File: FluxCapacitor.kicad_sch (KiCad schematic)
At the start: 21 parts, among them J1 Jack-DC, U1 OKI-78SR-5_1.5-W36-C, U2 ESP32_DEVBOARD

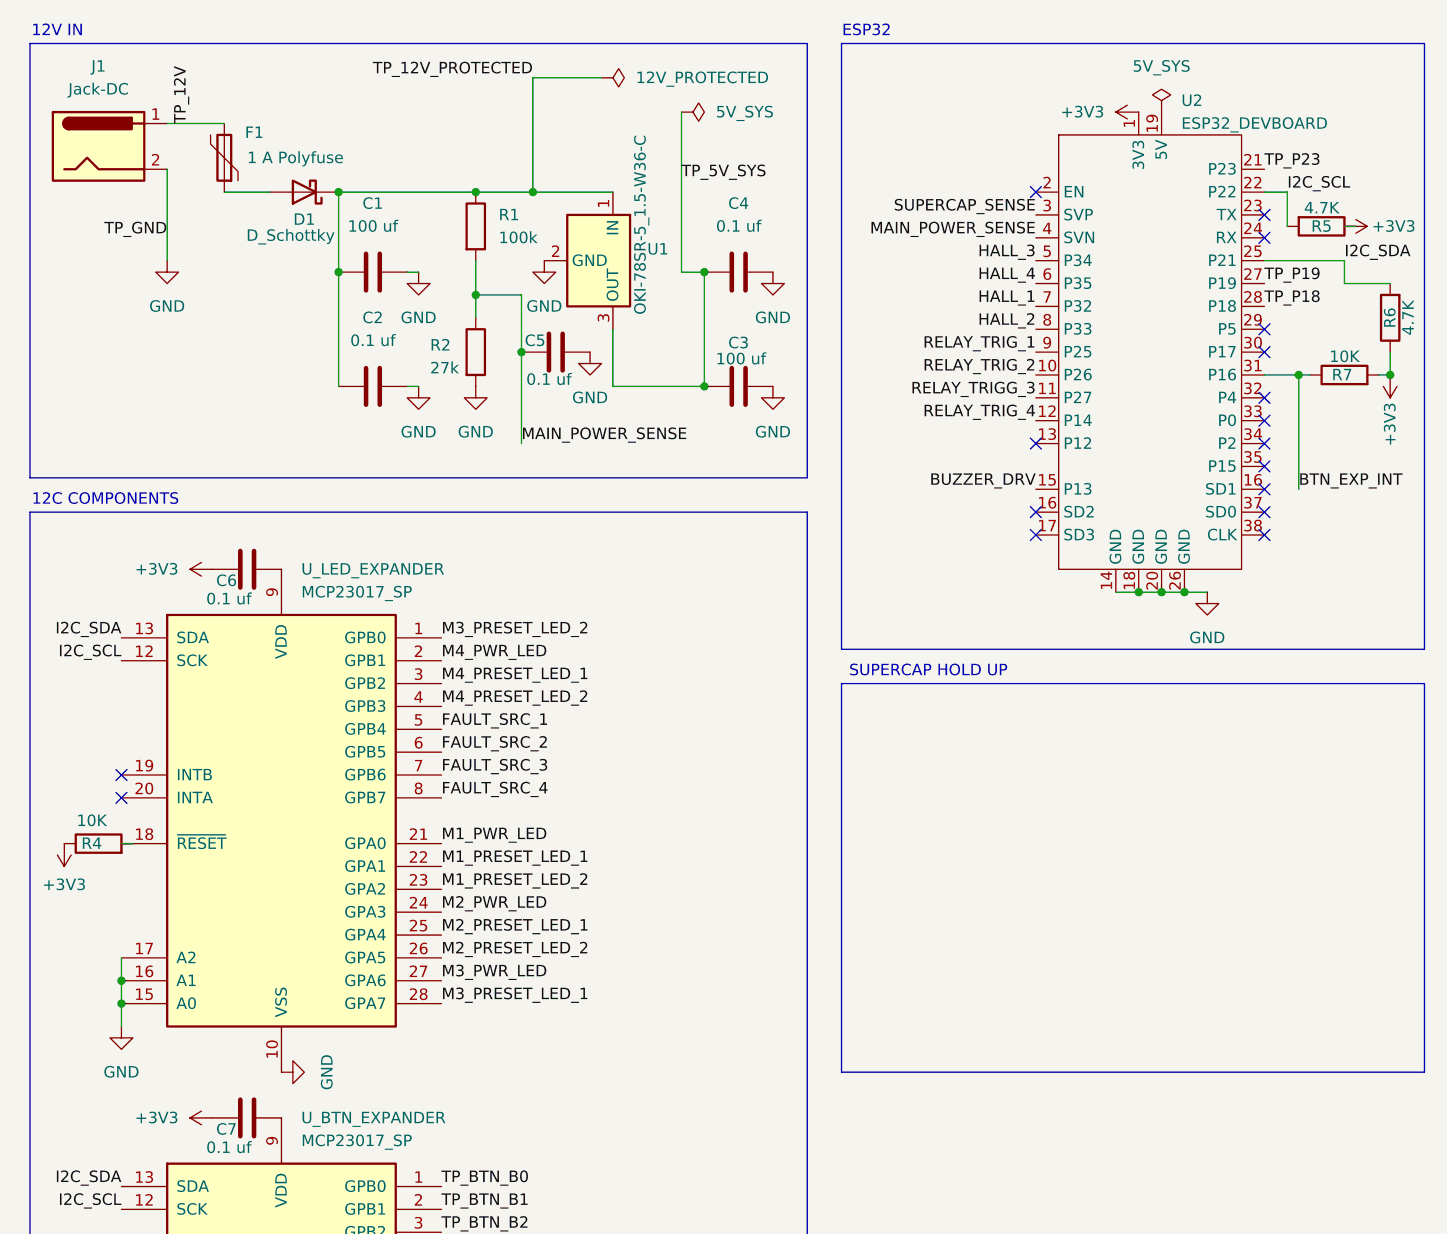
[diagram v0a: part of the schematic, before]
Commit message: Supercap commit
-changed 100uf bulk post buck to 47 because of supercap
-changed 5v sys test pad to 5v raw
-changed 5v_sys to 5v_raw from the buck
- supercap section
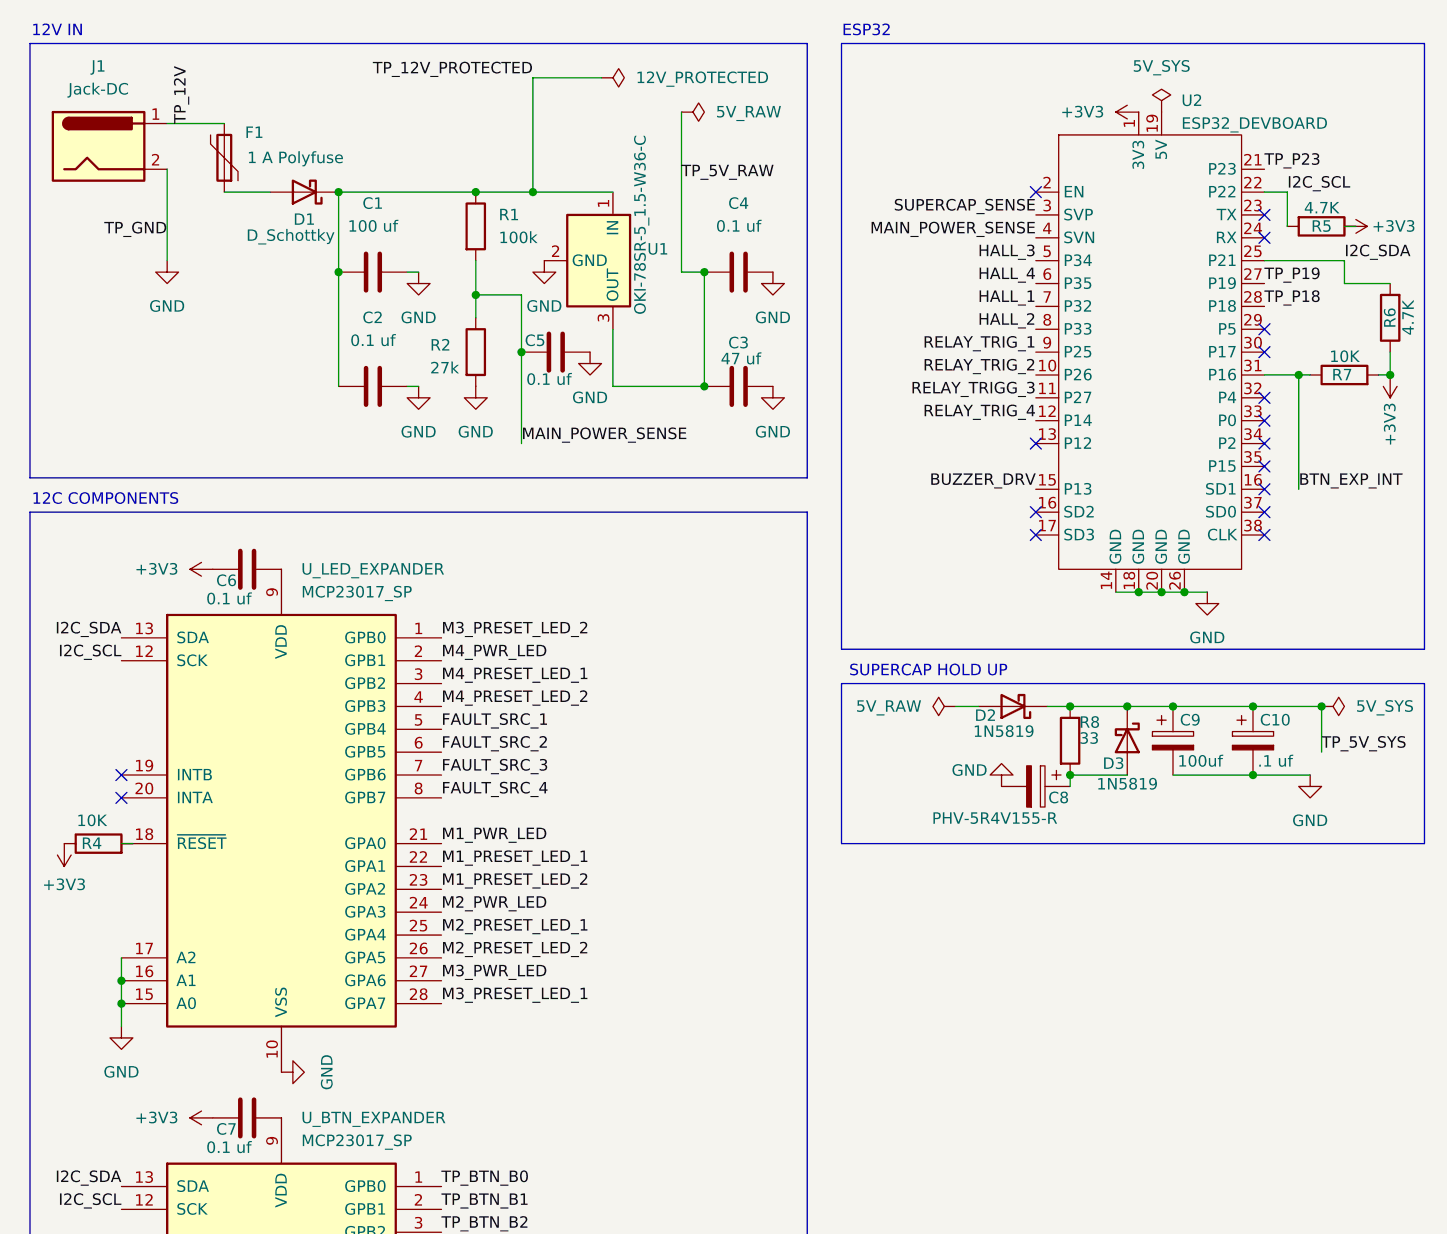
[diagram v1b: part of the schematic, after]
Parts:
- added C10: .1 uf, symbol Device:C_Polarized
- added C8: PHV-5R4V155-R, symbol Device:C_Polarized
- added C9: 100uf, symbol Device:C_Polarized
- added D2, D3: 1N5819, Diode_THT:D_DO-41_SOD81_P10.16mm_Horizontal, symbol Diode:1N5819
- added R8: 33, symbol Device:R
- C3: value 100 uf -> 47 uf
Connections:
- net GND: now also C10.2, C8.2, C9.2
- net TP_5V_SYS: now also C10.1, C9.1, D2.1 (K), D3.1 (K), R8.1; no longer C3.1, C4.1, U1.3 (OUT)
- new net: C8.1, D3.2 (A), R8.2
- new net TP_5V_RAW: C3.1, C4.1, U1.3 (OUT)

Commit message: cap symbol change
changed .1uf ceramic after supercap from polarized to unpolarized
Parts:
- removed C10: .1 uf, symbol Device:C_Polarized
- added C10: .1uf, symbol Device:C
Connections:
- net GND: now also C10.2
- net TP_5V_SYS: now also C10.1

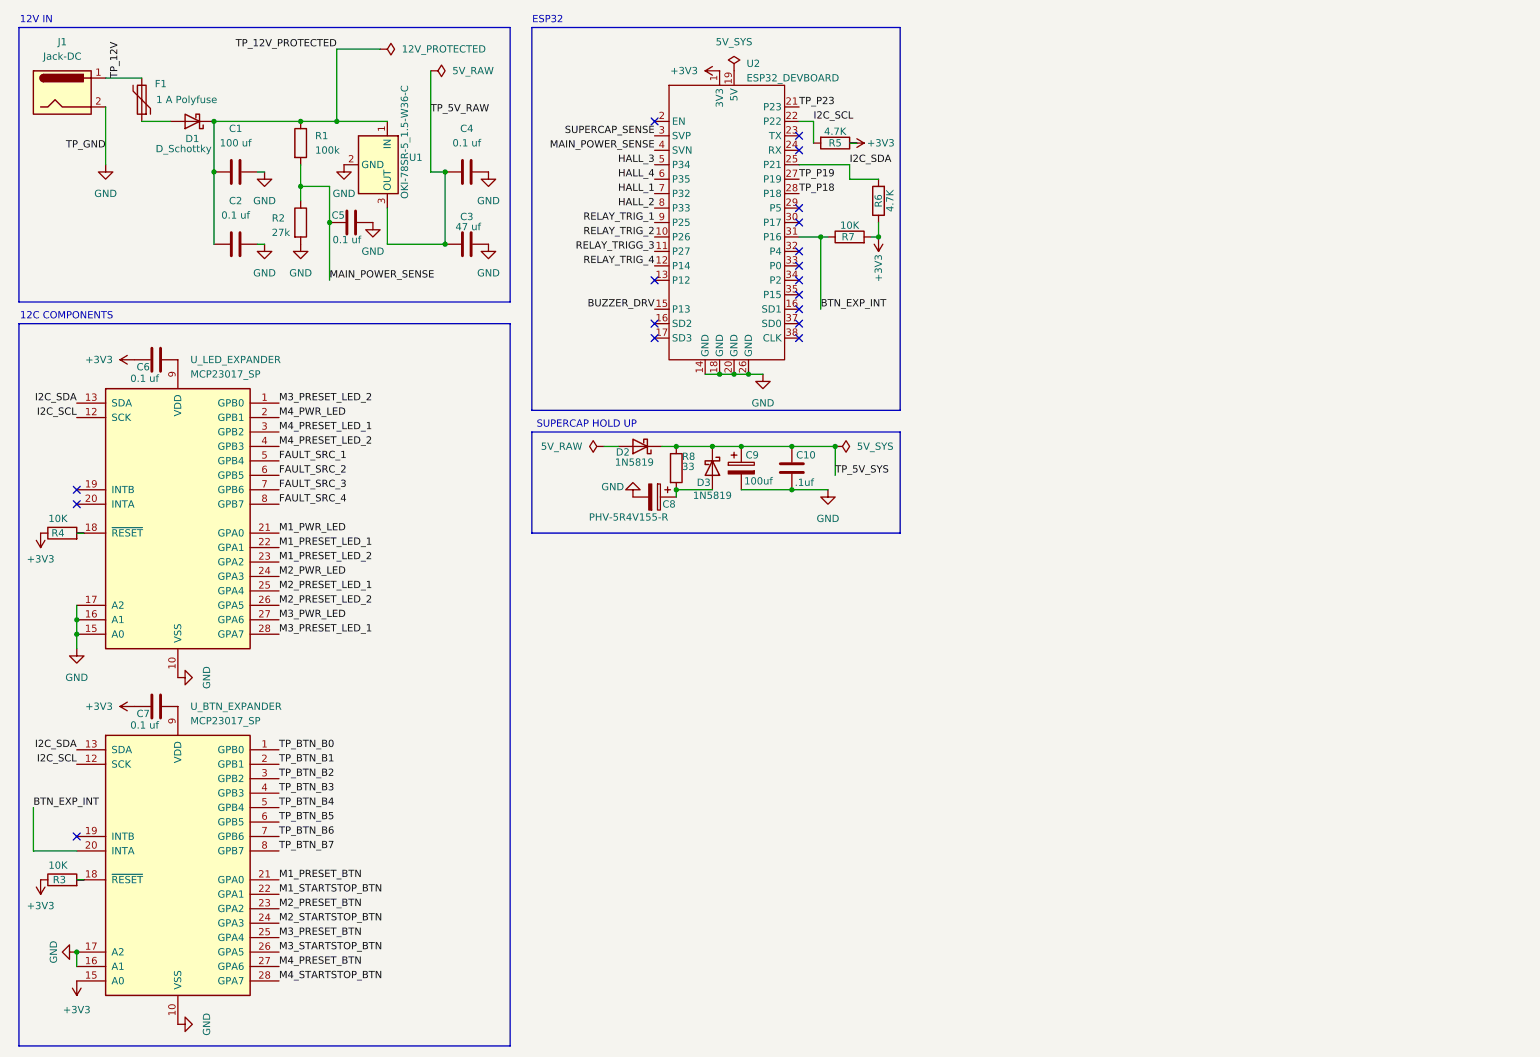
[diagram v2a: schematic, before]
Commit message: Treadmill Daughterboard Commit
Created treadmill daughterboard schematic, started wiring it up on the main page
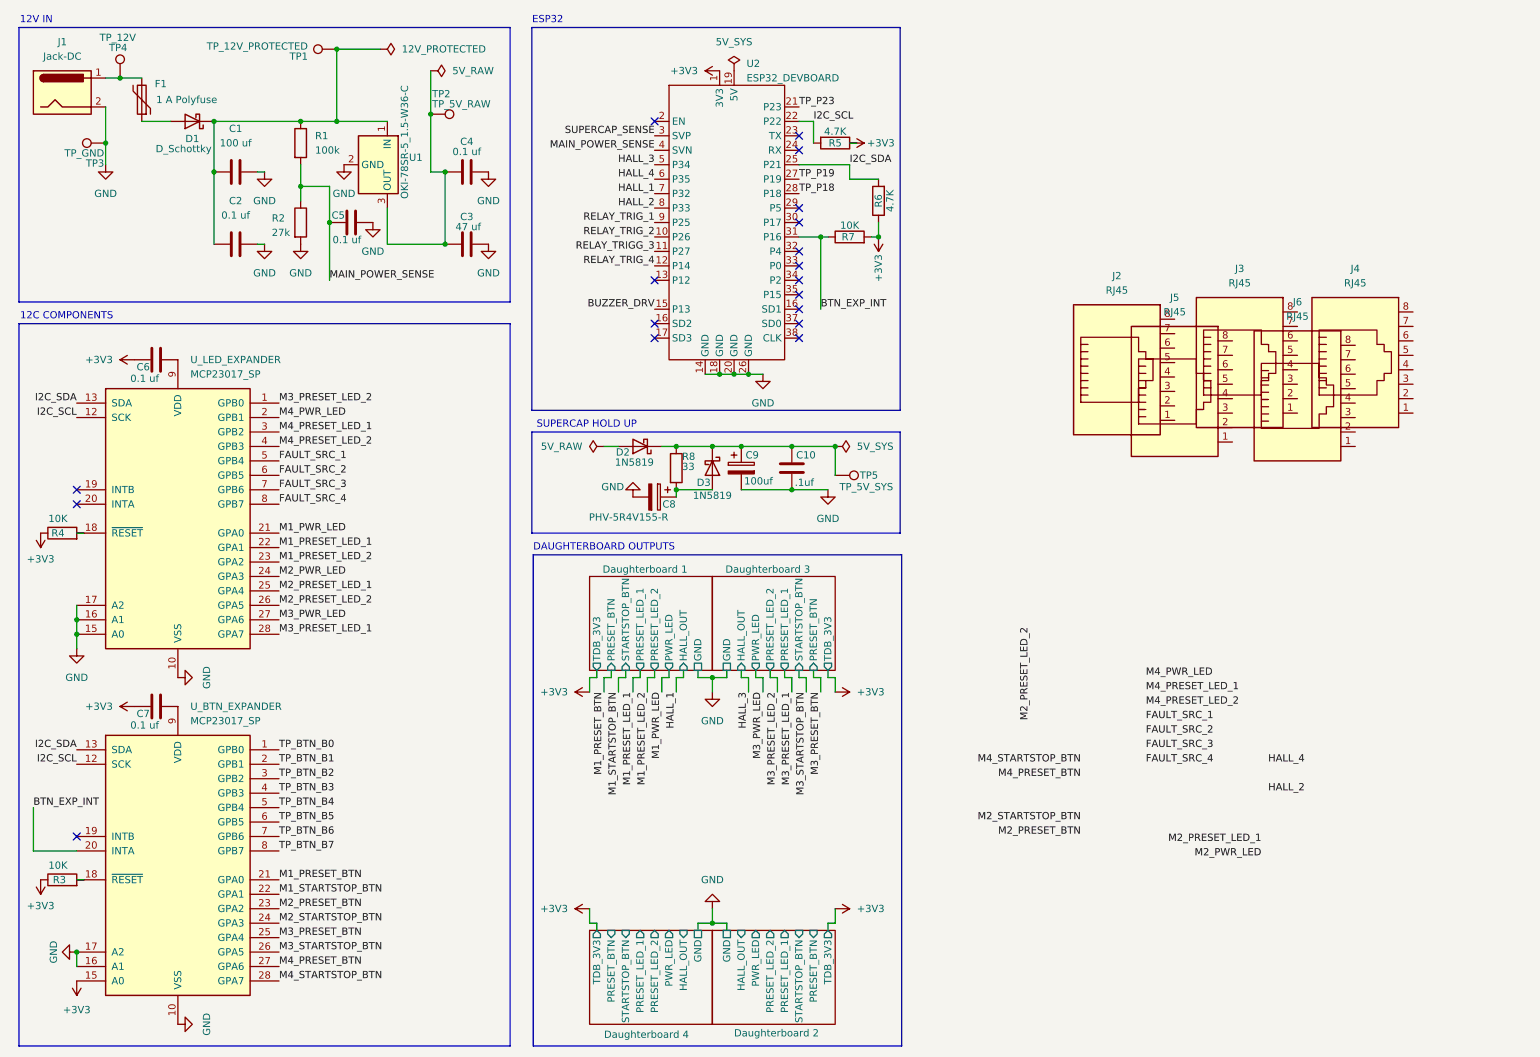
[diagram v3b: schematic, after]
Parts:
- added J2, J3, J4, J5, J6: RJ45, symbol Connector:RJ45
- added TP1: TP_12V_PROTECTED, symbol Connector:TestPoint
- added TP2: TP_5V_RAW, symbol Connector:TestPoint
- added TP3: TP_GND, symbol Connector:TestPoint
- added TP4: TP_12V, symbol Connector:TestPoint
- added TP5: TP_5V_SYS, symbol Connector:TestPoint
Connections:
- net GND: now also TP3.1
- net TP_12V: no longer names the net of F1.2, J1.1
- net TP_12V: now also TP4.1
- net TP_12V_PROTECTED: no longer names the net of C1.1, C2.1, D1.1 (K), R1.1, U1.1 (IN)
- net TP_12V_PROTECTED: now also TP1.1
- net TP_5V_RAW: no longer names the net of C3.1, C4.1, U1.3 (OUT)
- net TP_5V_RAW: now also TP2.1
- net TP_5V_SYS: no longer names the net of C10.1, C9.1, D2.1 (K), D3.1 (K), R8.1
- net TP_5V_SYS: now also TP5.1
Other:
- added sheet Daughterboard 1 (TreadmillDaughterboard.kicad_sch)
- added sheet Daughterboard 2 (TreadmillDaughterboard.kicad_sch)
- added sheet Daughterboard 3 (TreadmillDaughterboard.kicad_sch)
- added sheet Daughterboard 4 (TreadmillDaughterboard.kicad_sch)
- note added: "DAUGHTERBOARD OUTPUTS"

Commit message: Fixed Daughterboard Outputs Box
Replaced the TM hierarchical boxes with connectors
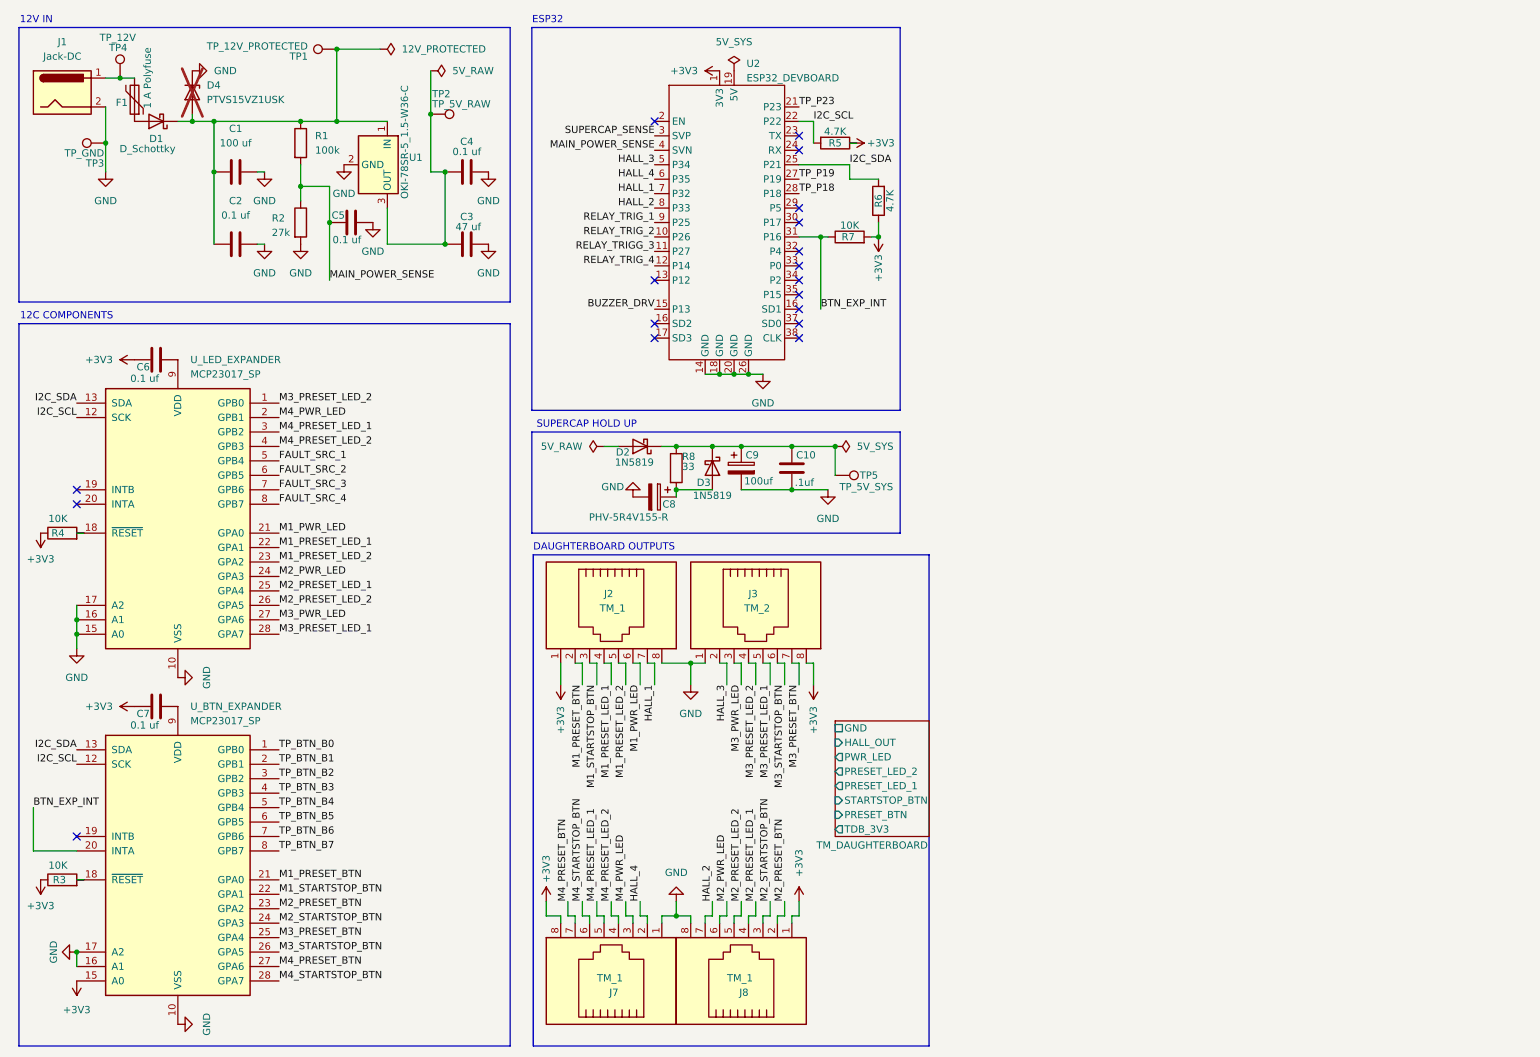
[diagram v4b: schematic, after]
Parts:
- removed J4, J5, J6: RJ45, symbol Connector:RJ45
- added D4: PTVS15VZ1USK, Diode_SMD:Nexperia_DSN1608-2_1.6x0.8mm, symbol Diode:PTVS15VZ1USK
- added J7, J8: TM_1, symbol Connector:RJ45
- J2: value RJ45 -> TM_1
- J3: value RJ45 -> TM_2
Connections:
- net +3V3: now also J2.1, J3.8, J7.8, J8.1
- net GND: now also J2.8, J3.1, D4.1 (K), J7.1, J8.8
- net HALL_1: now also J2.7
- net HALL_2: now also J8.7
- net HALL_3: now also J3.2
- net HALL_4: now also J7.2
- net M1_PRESET_BTN: now also J2.2
- net M1_PRESET_LED_1: now also J2.4
- net M1_PRESET_LED_2: now also J2.5
- net M1_PWR_LED: now also J2.6
- net M1_STARTSTOP_BTN: now also J2.3
- net M2_PRESET_BTN: now also J8.2
- net M2_PRESET_LED_1: now also J8.4
- net M2_PRESET_LED_2: now also J8.5
- net M2_PWR_LED: now also J8.6
- net M2_STARTSTOP_BTN: now also J8.3
- net M3_PRESET_BTN: now also J3.7
- net M3_PRESET_LED_1: now also J3.5
- net M3_PRESET_LED_2: now also J3.4
- net M3_PWR_LED: now also J3.3
- net M3_STARTSTOP_BTN: now also J3.6
- net M4_PRESET_BTN: now also J7.7
- net M4_PRESET_LED_1: now also J7.5
- net M4_PRESET_LED_2: now also J7.4
- net M4_PWR_LED: now also J7.3
- net M4_STARTSTOP_BTN: now also J7.6
- net at C1.1, C2.1, D1.1 (K)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: now also D4.2 (A)
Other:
- removed sheet Daughterboard 1
- removed sheet Daughterboard 2
- removed sheet Daughterboard 3
- removed sheet Daughterboard 4
- added sheet TM_DAUGHTERBOARD (TreadmillDaughterboard.kicad_sch)
- moved on the sheet: D1, F1, J2

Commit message: Reminder
Added a huge fix rj45 jack pin numbers label across the daughterboard outputs because the jack pins dont align with what should be connected to that pin number
also renamed the daughterboard outputs to tm daughterboard connections
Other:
- note added: "FIX RJ45 JACK PIN NUNMBERS"
- note added: "TM DAUGHTERBOARD CONNECTIONS"
- note removed: "DAUGHTERBOARD OUTPUTS"
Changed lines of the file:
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@@
 		)
 	)
-	(text "DAUGHTERBOARD OUTPUTS"
+	(text "FIX RJ45 JACK PIN NUNMBERS"
 		(exclude_from_sim no)
-		(at 118.11 106.68 0)
+		(at 136.144 130.048 0)
 		(effects
 			(font
+				(size 5 5)
+				(thickness 1)
+				(bold yes)
+				(color 31 255 0 1)
+			)
+		)
+	)
+	(text "TM DAUGHTERBOARD CONNECTIONS"
+		(exclude_from_sim no)
+		(at 121.92 106.934 0)
+		(effects
+			(font
